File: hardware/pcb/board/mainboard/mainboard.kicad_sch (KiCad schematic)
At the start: 145 parts, among them J1 Conn_Coaxial, J10 USB_C_Receptacle, J11 2908-05WB-MG, J2 USB_C_Receptacle_USB2.0_16P, J3 Conn_02x35_Odd_Even_MountingP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, J4 Conn_02x40_Odd_Even_MountingP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, J5 Conn_02x40_Odd_Even_MountingP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, J7 Conn_01x30, J8 Conn_01x30, Q1 BSS138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

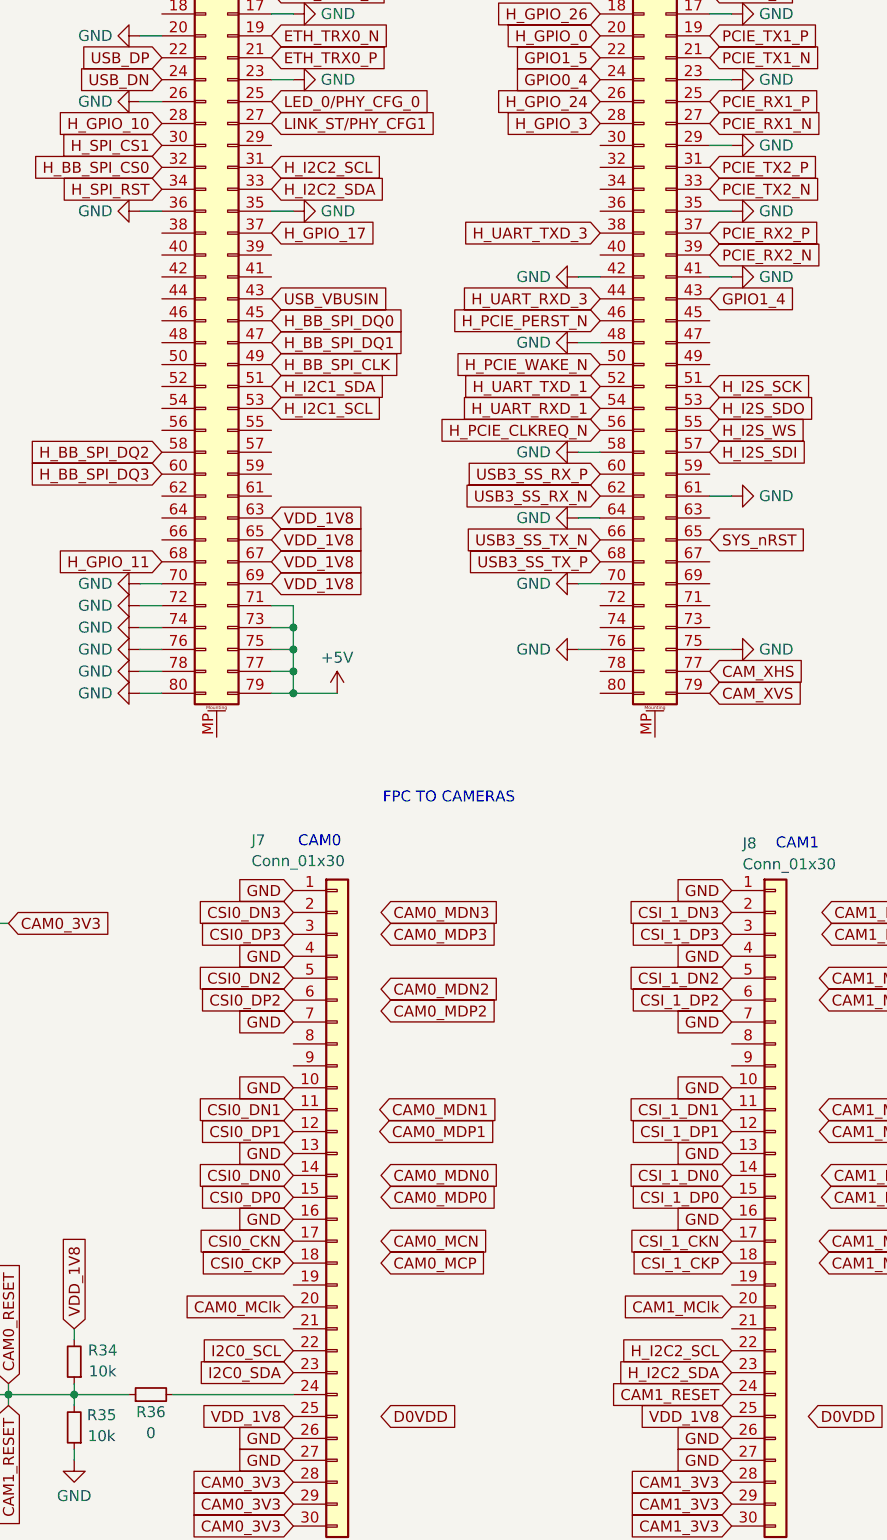
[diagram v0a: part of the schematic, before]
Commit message: cam0 MIPI pairs
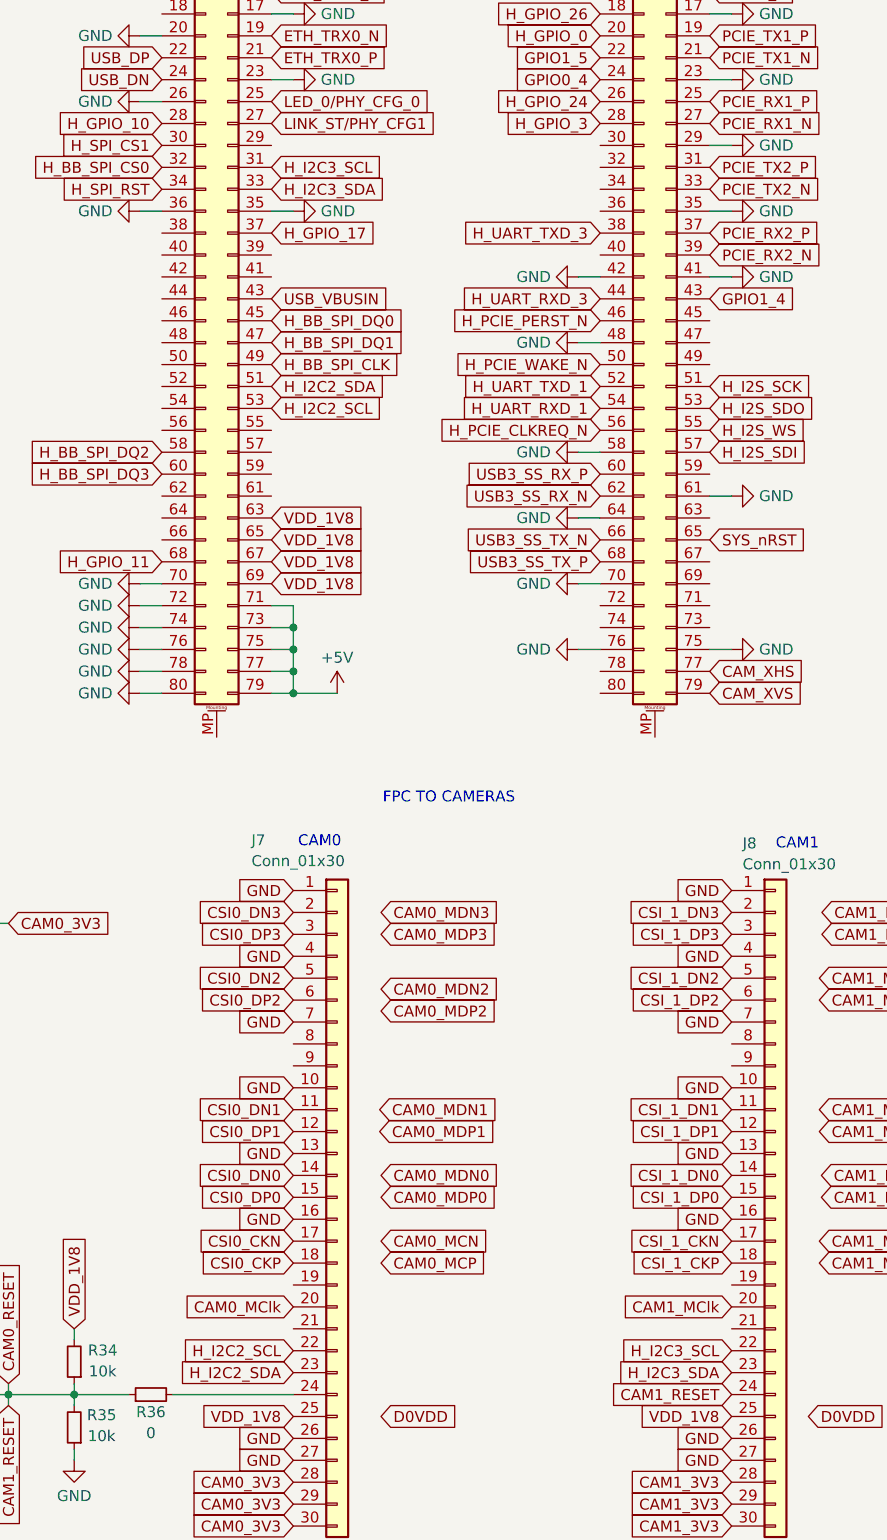
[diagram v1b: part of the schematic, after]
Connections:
- net H_I2C1_SCL is gone; now on net H_I2C2_SCL: J4.53 (Pin_53)
- net H_I2C1_SDA is gone; now on net H_I2C2_SDA: J4.51 (Pin_51)
- net I2C0_SCL is gone; now on net H_I2C2_SCL: J7.22 (Pin_22)
- net I2C0_SDA is gone; now on net H_I2C2_SDA: J7.23 (Pin_23)
- net H_I2C2_SCL: no longer J4.31 (Pin_31), J8.22 (Pin_22)
- net H_I2C2_SDA: no longer J4.33 (Pin_33), J8.23 (Pin_23)
- new net H_I2C3_SCL: J4.31 (Pin_31), J8.22 (Pin_22)
- new net H_I2C3_SDA: J4.33 (Pin_33), J8.23 (Pin_23)
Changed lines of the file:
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@@
 		)
 	)
-	(global_label "I2C0_SDA"
-		(shape input)
-		(at 449.58 351.79 180)
-		(fields_autoplaced yes)
-		(effects
-			(font
-				(size 1.27 1.27)
-			)
-			(justify right)
-		)
-		(property "Intersheetrefs" "${INTERSHEET_REFS}"
-			(at 437.7653 351.79 0)
-			(hide yes)
-			(show_name no)
-			(do_not_autoplace no)
-			(effects
-				(font
-					(size 1.27 1.27)
-				)
-				(justify right)
-			)
-		)
-	)
 	(global_label "H_GPIO_1"
 		(shape input)
@@
 		)
 	)
-	(global_label "H_I2C2_SCL"
+	(global_label "H_I2C3_SCL"
 		(shape input)
 		(at 447.04 212.09 0)
@@
 		)
 	)
+	(global_label "H_I2C2_SDA"
+		(shape input)
+		(at 449.58 351.79 180)
+		(fields_autoplaced yes)
+		(effects
+			(font
+				(size 1.27 1.27)
+			)
+			(justify right)
+		)
+		(property "Intersheetrefs" "${INTERSHEET_REFS}"
+			(at 435.4672 351.79 0)
+			(hide yes)
+			(show_name no)
+			(do_not_autoplace no)
+			(effects
+				(font
+					(size 1.27 1.27)
+				)
+				(justify right)
+			)
+		)
+	)
 	(global_label "GND"
 		(shape input)
@@
 		)
 	)
-	(global_label "H_I2C1_SCL"
+	(global_label "H_I2C2_SCL"
 		(shape input)
 		(at 447.04 240.03 0)
@@
 		)
 	)
-	(global_label "I2C0_SCL"
-		(shape input)
-		(at 449.58 349.25 180)
-		(fields_autoplaced yes)
-		(effects
-			(font
-				(size 1.27 1.27)
-			)
-			(justify right)
-		)
-		(property "Intersheetrefs" "${INTERSHEET_REFS}"
-			(at 437.8258 349.25 0)
-			(hide yes)
-			(show_name no)
-			(do_not_autoplace no)
-			(effects
-				(font
-					(size 1.27 1.27)
-				)
-				(justify right)
-			)
-		)
-	)
 	(global_label "CSI_1_DP2"
 		(shape input)
@@
 		)
 	)
-	(global_label "H_I2C1_SDA"
+	(global_label "H_I2C2_SDA"
 		(shape input)
 		(at 447.04 237.49 0)
@@
 		)
 	)
-	(global_label "H_I2C2_SDA"
+	(global_label "H_I2C3_SDA"
 		(shape input)
 		(at 500.38 351.79 180)
@@
 		)
 	)
+	(global_label "H_I2C2_SCL"
+		(shape input)
+		(at 449.58 349.25 180)
+		(fields_autoplaced yes)
+		(effects
+			(font
+				(size 1.27 1.27)
+			)
+			(justify right)
+		)
+		(property "Intersheetrefs" "${INTERSHEET_REFS}"
+			(at 435.5277 349.25 0)
+			(hide yes)
+			(show_name no)
+			(do_not_autoplace no)
+			(effects
+				(font
+					(size 1.27 1.27)
+				)
+				(justify right)
+			)
+		)
+	)
 	(global_label "H_I2S_SDI"
 		(shape input)
@@
 		)
 	)
-	(global_label "H_I2C2_SCL"
+	(global_label "H_I2C3_SCL"
 		(shape input)
 		(at 500.38 349.25 180)
@@
 		)
 	)
-	(global_label "H_I2C2_SDA"
+	(global_label "H_I2C3_SDA"
 		(shape input)
 		(at 447.04 214.63 0)

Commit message: dead reckoning routing
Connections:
- net +1V8: no longer C10.1, C17.2, C5.2, U2.12 (CS), U2.5 (VDDIO), U2.8 (VDD), U7.10 (Vdd_IO), U7.3 (~{CS})
- net B+: now also U5.7 (SRN); no longer U5.8 (SRP)
- net H_GPIO_10: now also TP4.1, U2.9 (INT2)
- net H_GPIO_11: now also TP11.1, U7.7 (DRDY)
- net H_GPIO_17: now also TP2.1, U2.4 (INT1)
- net H_GPIO_24: no longer TP4.1, U2.9 (INT2)
- net H_GPIO_26: no longer TP2.1, U2.4 (INT1)
- net H_GPIO_27: no longer TP11.1, U7.7 (DRDY)
- net H_I2C2_SCL: now also U2.13 (SCL), U5.2 (SCL), U7.1 (SCL/SPC)
- net H_I2C2_SDA: now also U2.14 (SDA), U5.1 (SDA), U7.4 (SDA/SDI/SDO)
- net SCL: no longer U2.13 (SCL), U5.2 (SCL), U7.1 (SCL/SPC)
- net SDA: no longer U2.14 (SDA), U5.1 (SDA), U7.4 (SDA/SDI/SDO)
- net VDD_1V8: now also C10.1, C17.2, C5.2, U2.12 (CS), U2.5 (VDDIO), U2.8 (VDD), U7.10 (Vdd_IO), U7.3 (~{CS})
- net at C9.1, R4.2, U5.6 (BAT): now also U5.8 (SRP); no longer U5.7 (SRN)
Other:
- note added: "# TODO - TP everything! - 0 ohm connections - WATCH FOR INVERSE PINS WHEN SWITCHING SIDE FOR CAM 0 / 1"
- note added: "# TODO USB_PD correct here?"
- note removed: "# TODO - check coax conn type for antennas - TP everything! - 0 ohm connections - add way for cam0 cam1 slave master operation? - TXS0102 logic lvl shifter - WATCH FOR INVERSE PINS WHEN SWITCHING SIDE FOR CAM 0 / 1 - transfer SOM based MIPI to CAM connection via FPC - CAM CLK crystal , 0 Ohm, 25 MHz, 25 ppm, 1.8V"
- moved on the sheet: TP4

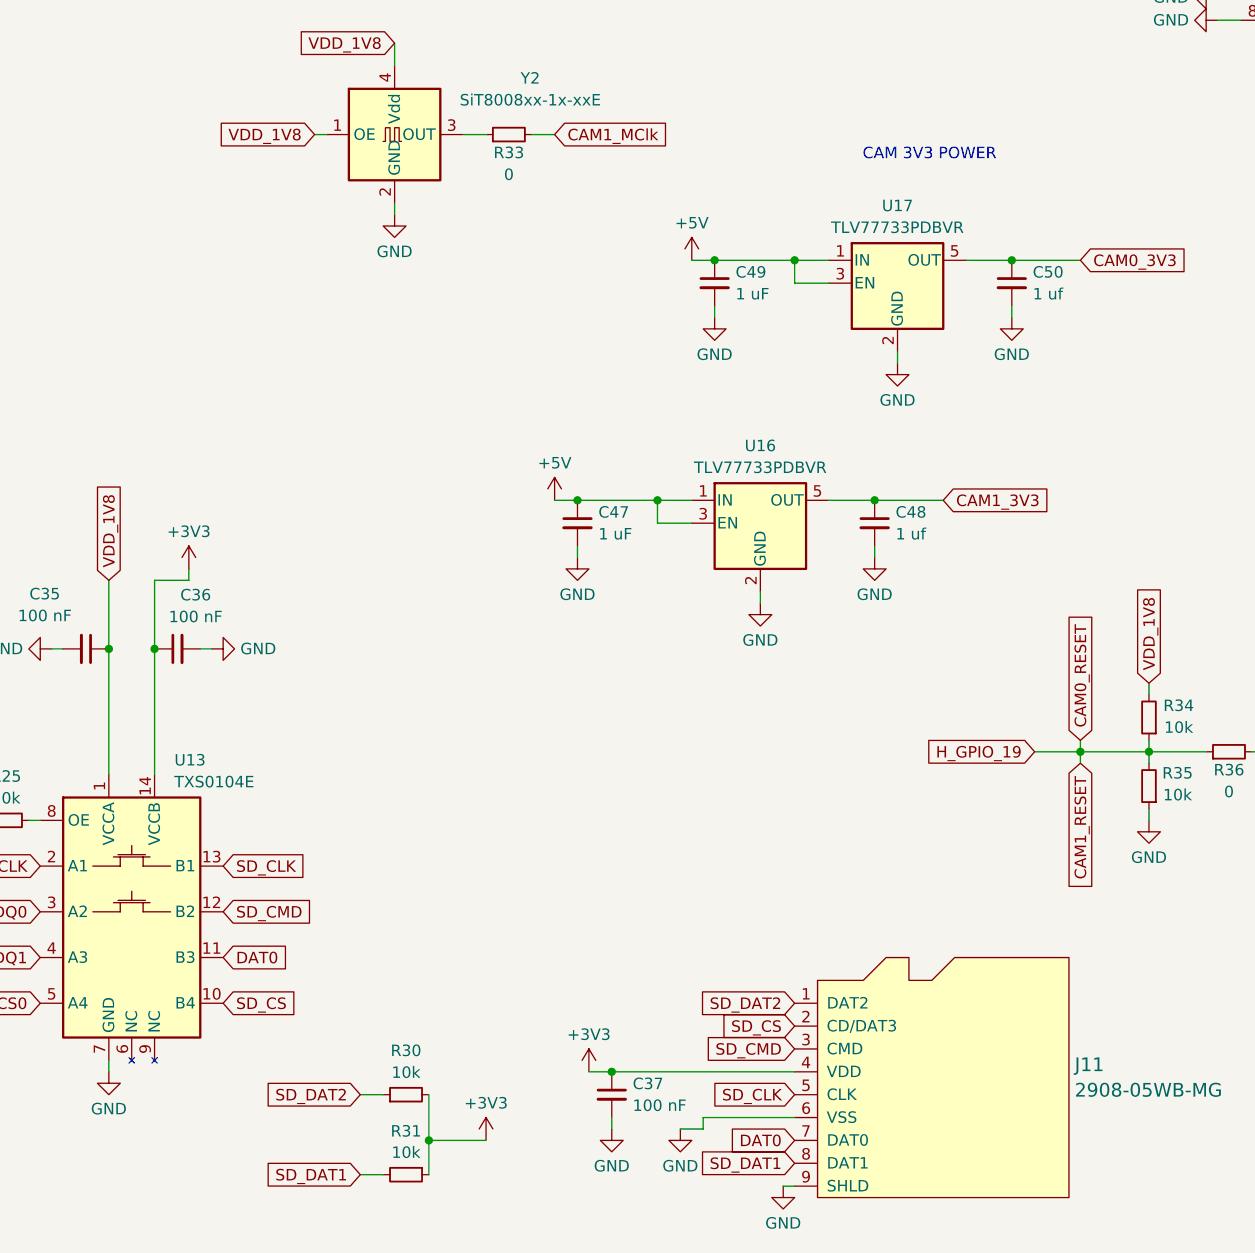
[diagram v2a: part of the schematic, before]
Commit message: SD card routing
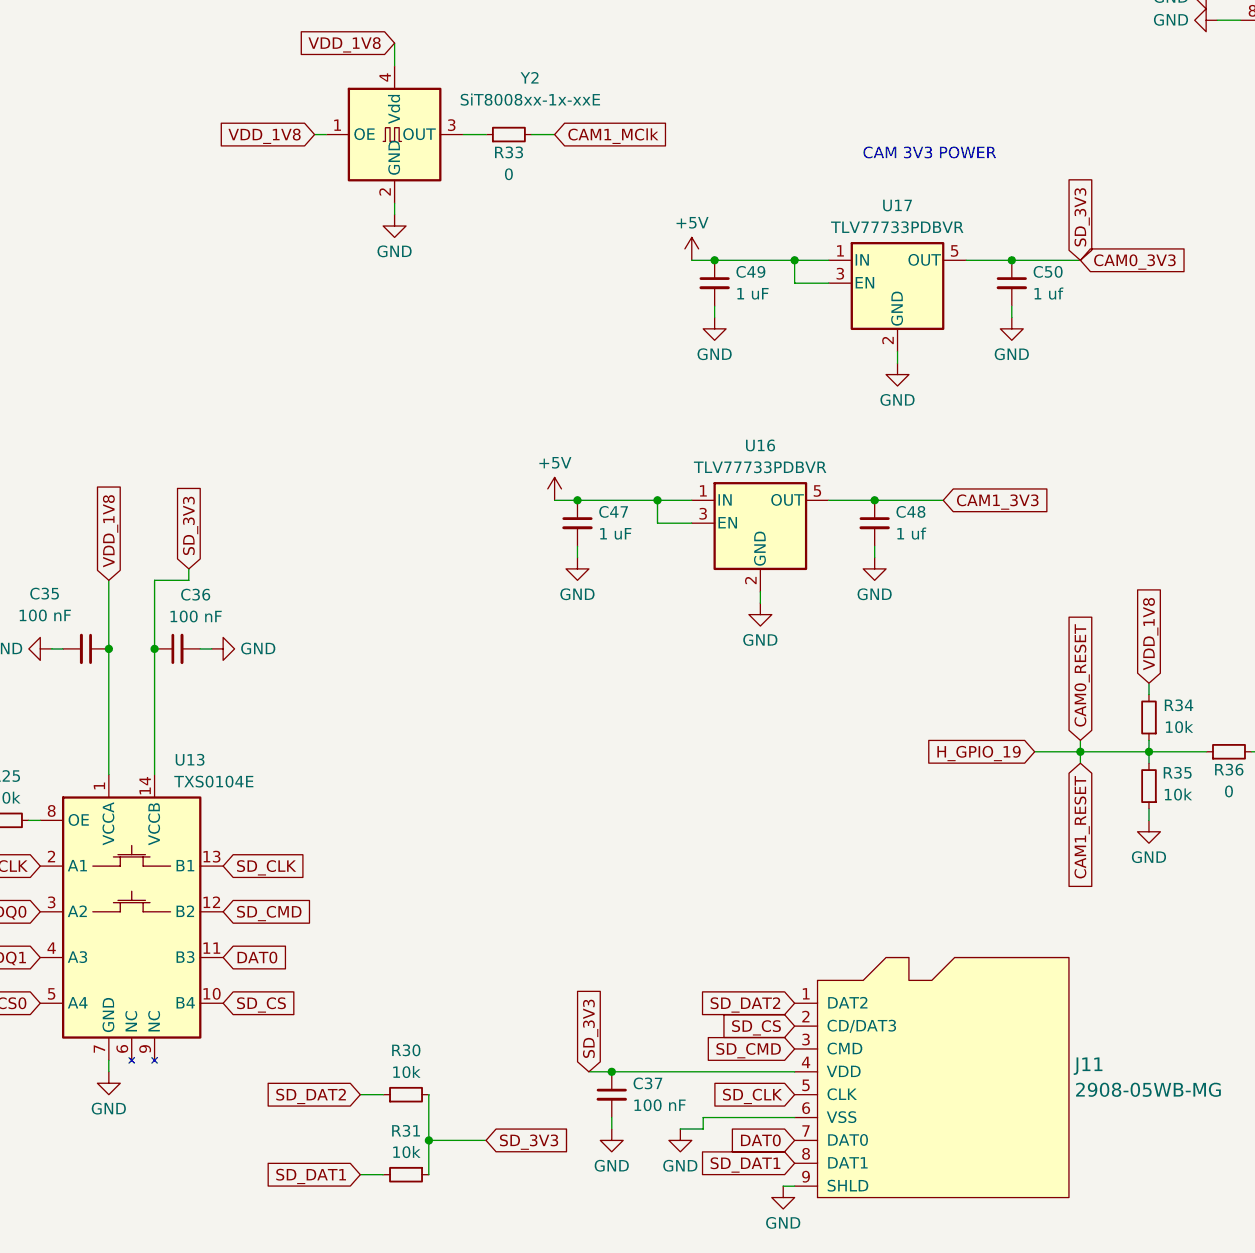
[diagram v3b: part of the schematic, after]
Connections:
- net +3V3 is gone; now on net CAM0_3V3: C36.1, C37.1, J11.4 (VDD), R30.2, R31.1, U13.14 (VCCB)
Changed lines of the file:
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@@
 		)
 	)
+	(global_label "SD_3V3"
+		(shape input)
+		(at 361.95 389.89 90)
+		(fields_autoplaced yes)
+		(effects
+			(font
+				(size 1.27 1.27)
+			)
+			(justify left)
+		)
+		(property "Intersheetrefs" "${INTERSHEET_REFS}"
+			(at 361.95 379.9501 90)
+			(hide yes)
+			(show_name no)
+			(do_not_autoplace no)
+			(effects
+				(font
+					(size 1.27 1.27)
+				)
+				(justify left)
+			)
+		)
+	)
 	(global_label "CSI_1_DP2"
 		(shape input)
@@
 		)
 	)
+	(global_label "SD_3V3"
+		(shape input)
+		(at 317.5 334.01 90)
+		(fields_autoplaced yes)
+		(effects
+			(font
+				(size 1.27 1.27)
+			)
+			(justify left)
+		)
+		(property "Intersheetrefs" "${INTERSHEET_REFS}"
+			(at 317.5 324.0701 90)
+			(hide yes)
+			(show_name no)
+			(do_not_autoplace no)
+			(effects
+				(font
+					(size 1.27 1.27)
+				)
+				(justify left)
+			)
+		)
+	)
 	(global_label "H_GPIO_11"
 		(shape input)
@@
 		)
 	)
+	(global_label "SD_3V3"
+		(shape input)
+		(at 416.56 299.72 90)
+		(fields_autoplaced yes)
+		(effects
+			(font
+				(size 1.27 1.27)
+			)
+			(justify left)
+		)
+		(property "Intersheetrefs" "${INTERSHEET_REFS}"
+			(at 416.56 289.7801 90)
+			(hide yes)
+			(show_name no)
+			(do_not_autoplace no)
+			(effects
+				(font
+					(size 1.27 1.27)
+				)
+				(justify left)
+			)
+		)
+	)
 	(global_label "H_UART_TXD_2"
 		(shape input)
@@
 		)
 	)
+	(global_label "SD_3V3"
+		(shape input)
+		(at 350.52 397.51 0)
+		(fields_autoplaced yes)
+		(effects
+			(font
+				(size 1.27 1.27)
+			)
+			(justify left)
+		)
+		(property "Intersheetrefs" "${INTERSHEET_REFS}"
+			(at 360.4599 397.51 0)
+			(hide yes)
+			(show_name no)
+			(do_not_autoplace no)
+			(effects
+				(font
+					(size 1.27 1.27)
+				)
+				(justify left)
+			)
+		)
+	)
 	(global_label "PCIE2_REF_CN_CLKN"
 		(shape input)
@@
 	)
 	(symbol
-		(lib_id "power:+3V3")
-		(at 317.5 334.01 0)
-		(mirror y)
-		(unit 1)
-		(body_style 1)
-		(exclude_from_sim no)
-		(in_bom yes)
-		(on_board yes)
-		(in_pos_files yes)
-		(dnp no)
-		(property "Reference" "#PWR0118"
-			(at 317.5 337.82 0)
-			(hide yes)
-			(show_name no)
-			(do_not_autoplace no)
-			(effects
-				(font
-					(size 1.27 1.27)
-				)
-			)
-		)
-		(property "Value" "+3V3"
-			(at 317.5 329.8769 0)
-			(show_name no)
-			(do_not_autoplace no)
-			(effects
-				(font
-					(size 1.27 1.27)
-				)
-			)
-		)
-		(property "Footprint" ""
-			(at 317.5 334.01 0)
-			(hide yes)
-			(show_name no)
-			(do_not_autoplace no)
-			(effects
-				(font
-					(size 1.27 1.27)
-				)
-			)
-		)
-		(property "Datasheet" ""
-			(at 317.5 334.01 0)
-			(hide yes)
-			(show_name no)
-			(do_not_autoplace no)
-			(effects
-				(font
-					(size 1.27 1.27)
-				)
-			)
-		)
-		(property "Description" "Power symbol creates a global label with name \"+3V3\""
-			(at 317.5 334.01 0)
-			(hide yes)
-			(show_name no)
-			(do_not_autoplace no)
-			(effects
-				(font
-					(size 1.27 1.27)
-				)
-			)
-		)
-		(pin "1"
-		)
-		(instances
-			(project "mainboard"
-				(path "/0d10df44-32de-4e15-8354-02c97578c850"
-					(reference "#PWR0118")
-					(unit 1)
-				)
-			)
-		)
-	)
-	(symbol
 		(lib_id "Device:C_Small")
 		(at 496.57 36.83 0)
@@
 	)
 	(symbol
-		(lib_id "power:+3V3")
-		(at 361.95 389.89 0)
-		(unit 1)
-		(body_style 1)
-		(exclude_from_sim no)
-		(in_bom yes)
-		(on_board yes)
-		(in_pos_files yes)
-		(dnp no)
-		(fields_autoplaced yes)
-		(property "Reference" "#PWR0135"
-			(at 361.95 393.7 0)
-			(hide yes)
-			(show_name no)
-			(do_not_autoplace no)
-			(effects
-				(font
-					(size 1.27 1.27)
-				)
-			)
-		)
-		(property "Value" "+3V3"
-			(at 361.95 385.7569 0)
-			(show_name no)
-			(do_not_autoplace no)
-			(effects
-				(font
-					(size 1.27 1.27)
-				)
-			)
-		)
-		(property "Footprint" ""
-			(at 361.95 389.89 0)
-			(hide yes)
-			(show_name no)
-			(do_not_autoplace no)
-			(effects
-				(font
-					(size 1.27 1.27)
-				)
-			)
-		)
-		(property "Datasheet" ""
-			(at 361.95 389.89 0)
-			(hide yes)
-			(show_name no)
-			(do_not_autoplace no)
-			(effects
-				(font
-					(size 1.27 1.27)
-				)
-			)
-		)
-		(property "Description" "Power symbol creates a global label with name \"+3V3\""
-			(at 361.95 389.89 0)
-			(hide yes)
-			(show_name no)
-			(do_not_autoplace no)
-			(effects
-				(font
-					(size 1.27 1.27)
-				)
-			)
-		)
-		(pin "1"
-		)
-		(instances
-			(project "mainboard"
-				(path "/0d10df44-32de-4e15-8354-02c97578c850"
-					(reference "#PWR0135")
-					(unit 1)
-				)
-			)
-		)
-	)
-	(symbol
 		(lib_id "power:GND")
 		(at 482.6 267.97 270)
@@
 					(unit 1)
 				)
-			)
-		)
-	)
-	(symbol
-		(lib_id "power:+3V3")
-		(at 350.52 397.51 0)
-		(unit 1)
-		(body_style 1)
-		(exclude_from_sim no)
-		(in_bom yes)
-		(on_board yes)
-		(in_pos_files yes)
-		(dnp no)
-		(fields_autoplaced yes)
-		(property "Reference" "#PWR0144"
-			(at 350.52 401.32 0)
-			(hide yes)
-			(show_name no)
-			(do_not_autoplace no)
-			(effects
-				(font
-					(size 1.27 1.27)
-				)
-			)
-		)
-		(property "Value" "+3V3"
-			(at 350.52 393.3769 0)
-			(show_name no)
-			(do_not_autoplace no)
-			(effects
-				(font
-					(size 1.27 1.27)
-				)
-			)
-		)
-		(property "Footprint" ""
-			(at 350.52 397.51 0)
-			(hide yes)
-			(show_name no)
-			(do_not_autoplace no)
-			(effects
-				(font
-					(size 1.27 1.27)
-				)
-			)
-		)
-		(property "Datasheet" ""
-			(at 350.52 397.51 0)
-			(hide yes)
-			(show_name no)
-			(do_not_autoplace no)
-			(effects
-				(font
-					(size 1.27 1.27)
-				)
-			)
-		)
-		(property "Description" "Power symbol creates a global label with name \"+3V3\""
-			(at 350.52 397.51 0)
-			(hide yes)
-			(show_name no)
-			(do_not_autoplace no)
-			(effects
-				(font
-					(size 1.27 1.27)
-				)
-			)
-		)
-		(pin "1"
-		)
-		(instances
-			(project "mainboard"
-				(path "/0d10df44-32de-4e15-8354-02c97578c850"
-					(reference "#PWR0144")
-					(unit 1)
-				)
